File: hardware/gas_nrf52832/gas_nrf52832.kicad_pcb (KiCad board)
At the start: 2 copper layers, 64 x 35 mm, 73 parts, among them IC1 NPM1100-QDAA-R, IC2 TCK106AG,LF, J1 J-link, J2 USB4515-GF-A_REVA, J3 Batt_SW, J4 Conn_01x03, Q1 DMC2400UV, Q2 FDV303N, Q3 FDV303N, U3 LPV811DBV, U4 LPV812DGK, U5 BME680, X1 32.768kHz

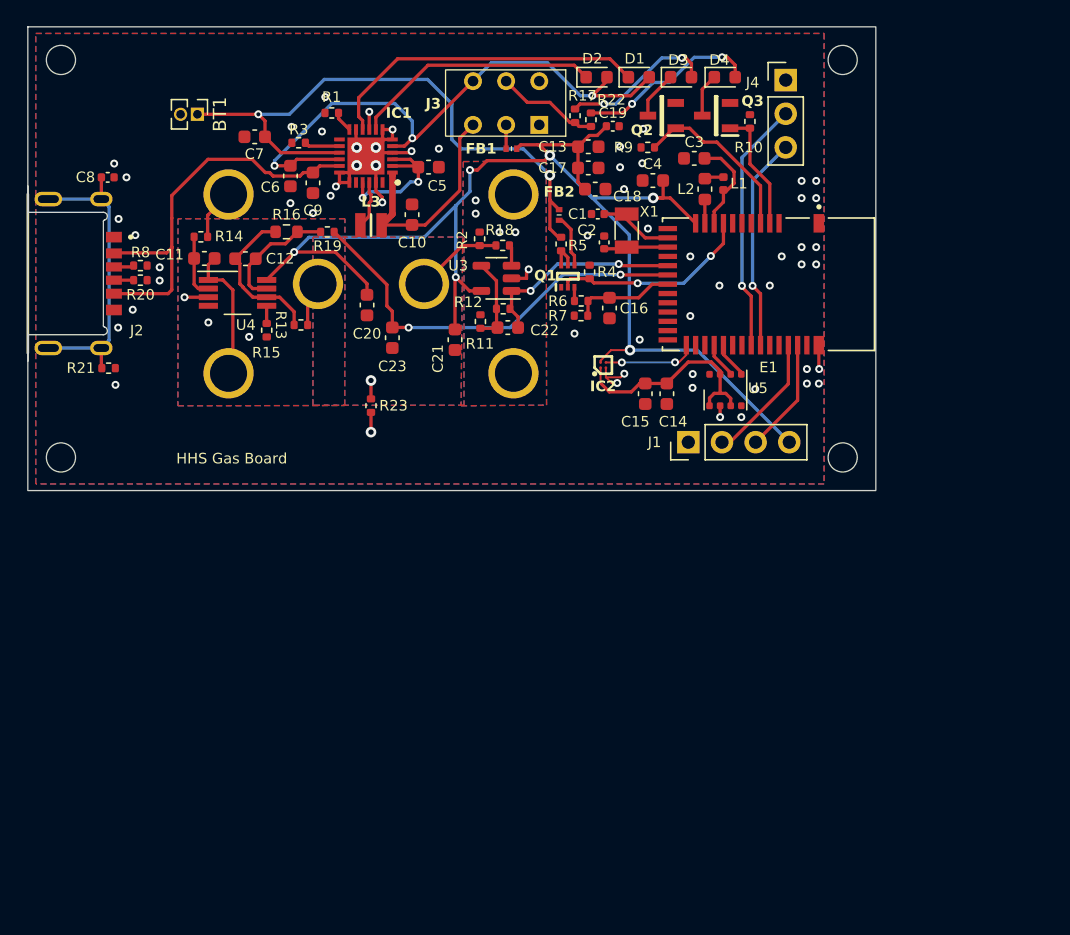
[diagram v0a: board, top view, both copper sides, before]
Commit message: hw: fix sensor circuit & fix ERC Error
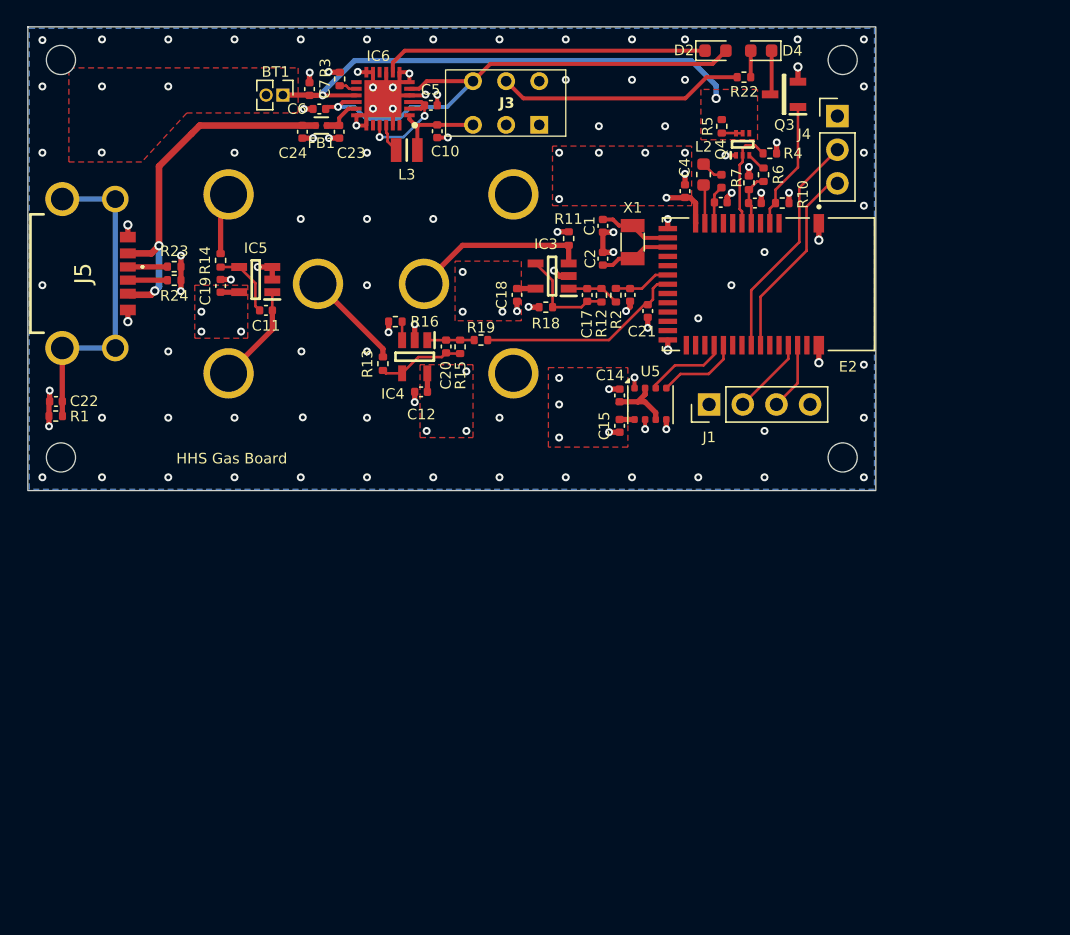
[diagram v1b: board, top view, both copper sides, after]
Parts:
- removed C8: 4.7nF, Capacitor_SMD:C_0402_1005Metric
- removed C9: 2.2uF, Capacitor_SMD:C_0603_1608Metric
- removed D1: L0603R, LED_SMD:LED_0603_1608Metric
- removed D3: L0603Y, LED_SMD:LED_0603_1608Metric
- removed E1: MDBT42Q-512KV2, MDBT42Q-512KV2:RAYTAC_MDBT42Q-512KV2
- removed FB2: BLM15PE121SH1D, BLM15PE121SH1D:NFZ15SG152SN10B
- removed IC1: NPM1100-QDAA-R, NPM1100-QDAA:QFN50P400X400X90-25N-D
- removed IC2: TCK106AG,LF, TCK106AG,LF:BGA4C40P2X2_79X79X59
- removed J2: USB4515-GF-A_REVA, USB4515-GF-A_REVA:GCT_USB4515-GF-A_REVA
- removed Q1: DMC2400UV, DMC2400UV:SOTFL50P162X60-6N
- removed Q2: FDV303N, FDV303N:SOT96P237X111-3N
- removed R17: 150, Resistor_SMD:R_0402_1005Metric
- removed R20, R8: 5.1k, Resistor_SMD:R_0402_1005Metric
- removed R21, R9: 1M, Resistor_SMD:R_0402_1005Metric
- removed U3: LPV811DBV, Package_TO_SOT_SMD:SOT-23-5
- removed U4: LPV812DGK, Package_SO:VSSOP-8_3.0x3.0mm_P0.65mm
- added C24: 100nF, Capacitor_SMD:C_0402_1005Metric, F.Cu at (110.1, 83.4)
- added E2: MDBT42Q-512KV2, MDBT42Q-512KV2:RAYTAC_MDBT42Q-512KV2, F.Cu at (145.3, 94.9)
- added IC3: LPV821DBVR, LPV821DBVR:SOT95P280X145-5N, F.Cu at (129.0, 94.3)
- added IC4: LPV821DBVR, LPV821DBVR:SOT95P280X145-5N, F.Cu at (118.6, 100.4)
- added IC5: LPV821DBVR, LPV821DBVR:SOT95P280X145-5N, F.Cu at (106.6, 94.6)
- added IC6: NPM1100-QDAA-R, NPM1100-QDAA-R:QFN50P400X400X90-25N-D, F.Cu at (116.2, 80.9)
- added J5: USB4515-GF-A, USB4515-GF-A_REVA:USB4515GFA, F.Cu at (93.0, 94.1)
- added Q4: DMC2400UV, DMC2400UV:SOTFL50P162X60-6N, F.Cu at (143.3, 84.4)
- added R24: 5.1k, Resistor_SMD:R_0402_1005Metric, F.Cu at (100.5, 94.6)
- C10, C11, C14, C15, C16, C18, C3, C4, C5, C6, C7: footprint Capacitor_SMD:C_0603_1608Metric -> Capacitor_SMD:C_0402_1005Metric
- C12: value 1.0uF -> 0.1uF; footprint Capacitor_SMD:C_0603_1608Metric -> Capacitor_SMD:C_0402_1005Metric
- C13: value 10uF -> 4.7uF; footprint Capacitor_SMD:C_0603_1608Metric -> Capacitor_SMD:C_0402_1005Metric
- C17: value 1.0uF -> 4.7uF; footprint Capacitor_SMD:C_0603_1608Metric -> Capacitor_SMD:C_0402_1005Metric
- C19: value 4.7nF -> 0.1uF
- C20: value 0.1uF -> 1.0uF; footprint Capacitor_SMD:C_0603_1608Metric -> Capacitor_SMD:C_0402_1005Metric
- C21: value 0.1uF -> 4.7uF; footprint Capacitor_SMD:C_0603_1608Metric -> Capacitor_SMD:C_0402_1005Metric
- C22: value 0.1uF -> 4.7nF; footprint Capacitor_SMD:C_0603_1608Metric -> Capacitor_SMD:C_0402_1005Metric
- C23: value 1.0uF -> 10nF; footprint Capacitor_SMD:C_0603_1608Metric -> Capacitor_SMD:C_0402_1005Metric
- FB1: value BLM15PE121SH1D -> 120R/0.9A; footprint BLM15PE121SH1D:NFZ15SG152SN10B -> MURATA_BLM15PE121SH1D:MURATA_BLM15PE121SH1D_0
- R1: value 0 -> 1M
- R11: value 10.7 -> 100
- R12: value 2k -> 2M
- R14: value 10 -> 10k
- R15: value 10 -> 150k
- R16: value 150k -> 10; footprint Resistor_SMD:R_0603_1608Metric -> Resistor_SMD:R_0402_1005Metric
- R18: value 10.7 -> 10k
- R19: value 49.9k -> 10k
- R2: value 100 -> 10k
- R23: value 0 -> 5.1k
- moved C22 34.6 mm to (91.5, 103.8)
- moved C19 32.0 mm to (104.0, 95.0), turned to -90 degrees
- moved R1 30.9 mm to (91.5, 104.9)
- moved R23 18.2 mm to (100.5, 93.6), turned to 0 degrees
- moved R6 16.7 mm to (144.9, 86.7), turned to 90 degrees
- moved C12 16.6 mm to (119.1, 103.0), turned to 0 degrees
- moved R4 16.3 mm to (145.4, 85.0), turned to 0 degrees
- moved R7 16.2 mm to (143.8, 87.3), turned to -90 degrees
- moved C23 16.1 mm to (112.9, 83.4)
- moved R5 15.0 mm to (141.8, 83.0)
- moved C21 14.7 mm to (136.2, 97.0)
- moved R15 14.6 mm to (122.0, 99.7), turned to -90 degrees
- moved FB1 14.5 mm to (111.5, 83.0)
- moved R19 14.2 mm to (123.6, 99.1)
- moved C16 13.5 mm to (144.3, 88.8), turned to 0 degrees
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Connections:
- C11 pad 1: Net-(U4A--) -> Net-(IC5-OUT)
- C11 pad 2: Net-(C11-Pad2) -> Net-(IC5--IN)
- C12 pad 1: Net-(C12-Pad1) -> GND
- C12 pad 2: Net-(U4B--) -> VDD_nRF
- C13 pad 1: VDD_nRF -> GND
- C13 pad 2: GND -> O2_MON
- C14 pad 2: VDD_BME -> VDD_nRF
- C15 pad 2: VDD_BME -> VDD_nRF
- C17 pad 1: VDD_nRF -> Net-(IC3-OUT)
- C17 pad 2: GND -> Net-(IC3--IN)
- C18 pad 1: VDD_nRF -> GND
- C18 pad 2: GND -> VDD_nRF
- C19 pad 1: VDD_nRF -> GND
- C19 pad 2: GND -> VDD_nRF
- C20 pad 1: GNDA -> Net-(IC4-OUT)
- C20 pad 2: VDD_nRF -> Net-(IC4--IN)
- C21 pad 1: GNDA -> GND
- C21 pad 2: VDD_nRF -> GAS_MON
- C22 pad 1: Net-(U3--) -> GND
- C22 pad 2: O2_MON -> Net-(C22-Pad2)
- C23 pad 1: GNDA -> GND
- C23 pad 2: GAS_MON -> VBUS
- FB1 pad 1: +3V0 -> Net-(J5-VBUS_1)
- FB1 pad 2: VDD_nRF -> VBUS
- J3 pad 2: +3V0 -> VDD_nRF
- R1 pad 1: Net-(IC1-ICHG) -> Net-(C22-Pad2)
- R11 pad 1: Net-(U3--) -> Net-(IC3-+IN)
- R11 pad 2: GNDA -> GND
- R12 pad 1: Net-(U3--) -> Net-(IC3-OUT)
- R12 pad 2: O2_MON -> Net-(IC3--IN)
- R13 pad 1: Net-(U4B--) -> Net-(IC4--IN)
- R14 pad 1: Net-(U4A--) -> Net-(IC5--IN)
- R15 pad 1: GNDA -> Net-(IC4-OUT)
- R15 pad 2: Net-(U4B-+) -> Net-(IC4--IN)
- R16 pad 1: Net-(C12-Pad1) -> Net-(IC4-+IN)
- R16 pad 2: Net-(U4B--) -> GND
- R18 pad 1: Net-(R18-Pad1) -> GND
- R18 pad 2: Net-(U3-+) -> Net-(IC3--IN)
- R19 pad 1: Net-(C12-Pad1) -> Net-(IC4-OUT)
- R2 pad 1: Net-(R18-Pad1) -> Net-(IC3-OUT)
- R2 pad 2: GNDA -> O2_MON
- R23 pad 1: GNDA -> Net-(J5-CC1)
- R6 pad 2: BAT_MON_TP -> Net-(Q4-D2)
- U1 pad +ve: Net-(R18-Pad1) -> Net-(IC3-+IN)
- U1 pad -ve: GNDA -> GND
- U2 pad C: Net-(C11-Pad2) -> Net-(IC5-OUT)
- U5 pad 2: VDD_BME -> VDD_nRF
- U5 pad 6: VDD_BME -> VDD_nRF
- U5 pad 8: VDD_BME -> VDD_nRF
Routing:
- net VDD_nRF: track 102.8 -> 14.3 mm, vias 6 -> 18
- net GND: track 31.1 -> 63.0 mm, vias 59 -> 112
- net VBUS: track 30.8 -> 3.11 mm
- net Net-(J5-VBUS_1): track 0.00 -> 27.7 mm, vias 0 -> 2
- net Net-(D1-K): track 24.7 -> 0.00 mm
- net Net-(C22-Pad2): track 0.00 -> 24.4 mm
- net Net-(C8-Pad2): track 22.9 -> 0.00 mm
- net VDD_BME: track 16.4 -> 0.00 mm
- net GAS_MON: track 31.5 -> 15.8 mm, vias 2 -> 0
- net Net-(IC3-+IN): track 0.00 -> 13.5 mm
- net LOW_BATT: track 13.2 -> 0.00 mm
- net Net-(U4B--): track 11.9 -> 0.00 mm
- net Net-(D4-A): track 13.8 -> 2.00 mm, vias 2 -> 0
- net Net-(D3-A): track 11.6 -> 0.00 mm, vias 2 -> 0
- net O2_MON: track 15.8 -> 4.51 mm, vias 2 -> 0
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- added copper zone on In1.Cu, net GND
- added copper zone on F.Cu, net VBAT
- added copper zone on F.Cu, net VDD_nRF
- added copper zone on In2.Cu, net VDD_nRF
- removed copper zone on F.Cu, net GND
- removed copper zone on B.Cu, net GNDA
- removed copper zone on F.Cu, net GNDA
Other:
- copper layers 2 -> 4

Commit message: feat: hw revision 1.0.2
Rev 1.0.2
- Oxygen Sensor
	- Voltage Amplification Ratio AdjustmentR18(10.7 -> 10k), R12(2.0k -> 2M)
	-> Reduce Current Consumption
	- Addition of lowpass filter for Noise Reduction
- Gas Sensor
	- Addition of lowpass filter for Noise Reduction
- 2 Layter -> 4 Layer
- hansam digitec requirement
	- If USB and RC are very close, errors may occur
	so increase the distance (R1, R23, R24, C22)
- BME680 Sensor Enable ctrl remove
- 32k Crystal Layout fix
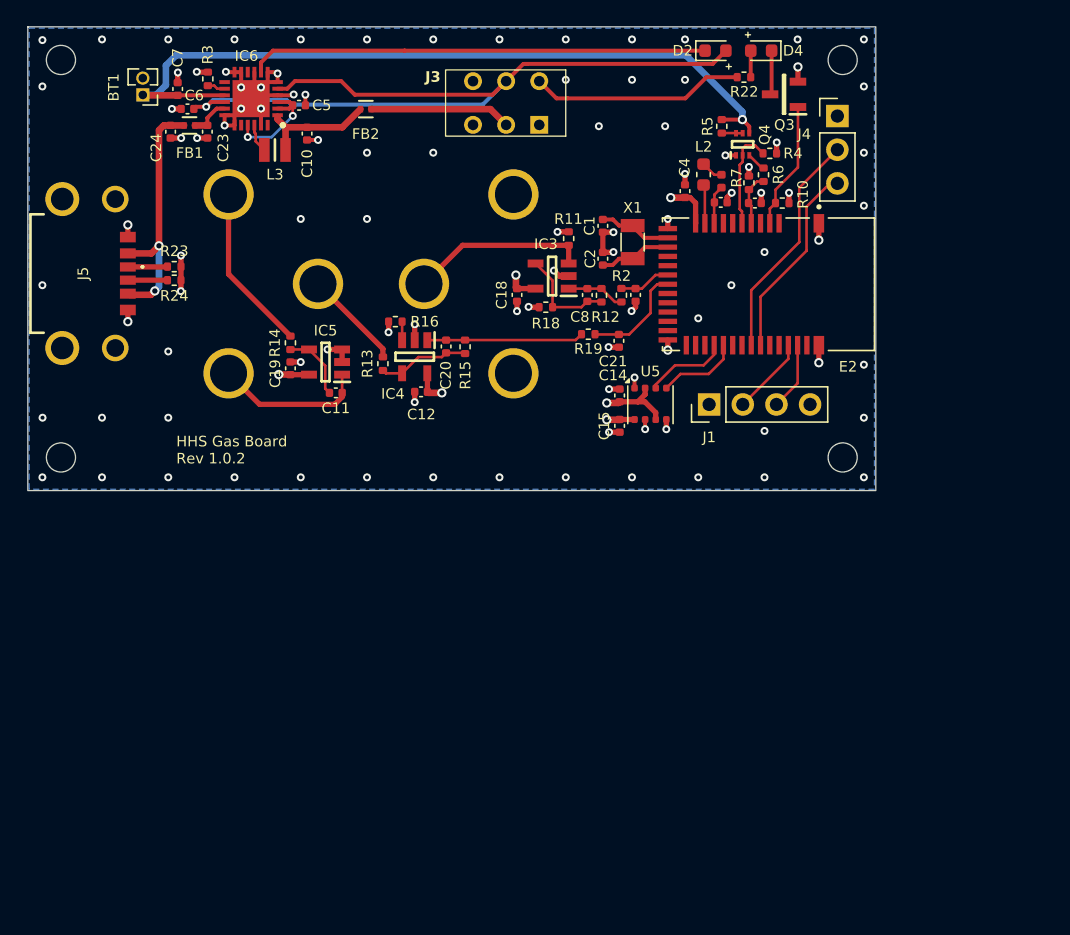
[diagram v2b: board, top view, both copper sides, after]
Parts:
- removed C17: 4.7uF, Capacitor_SMD:C_0402_1005Metric
- removed C22: 4.7nF, Capacitor_SMD:C_0402_1005Metric
- removed R1: 1M, Resistor_SMD:R_0402_1005Metric
- added C8: 1uF, Capacitor_SMD:C_0402_1005Metric, F.Cu at (131.6, 95.7)
- added FB2: 120R/0.9A, MURATA_BLM15PE121SH1D:MURATA_BLM15PE121SH1D_0, F.Cu at (114.9, 81.7)
- C11, C12, C14, C15, C16, C18, C19: value 0.1uF -> 100nF
- C13, C21: value 4.7uF -> 1uF
- C20, C3, C7: value 1.0uF -> 1uF
- D2: value L0603O -> L0603R
- Q4: value DMC2400UV -> DMC2400UV-7
- R14: value 10k -> 10
- R15: value 150k -> 100k
- R19, R2: value 10k -> 49.9k
- moved BT1 10.6 mm to (98.1, 80.6), turned to 180 degrees
- moved C23 9.95 mm to (103.0, 83.4)
- moved C24 9.95 mm to (100.2, 83.4)
- moved C6 9.95 mm to (101.5, 81.7)
- moved C7 9.95 mm to (100.7, 80.2)
- moved FB1 9.95 mm to (101.6, 82.9)
- moved IC6 9.95 mm to (106.2, 80.9)
- moved L3 9.95 mm to (108.0, 84.8)
- moved R3 9.95 mm to (103.0, 79.4)
- moved C5 9.95 mm to (109.9, 81.4)
- moved C10 9.83 mm to (110.5, 83.6)
- moved C19 8.16 mm to (109.2, 101.3)
- moved IC5 8.16 mm to (111.9, 100.8)
- moved C11 8.16 mm to (112.6, 103.1)
- moved R14 8.16 mm to (109.2, 99.3)
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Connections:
- E2 pad 25: SENSOR_EN -> unconnected-(E2-P0.11-Pad25)
- J3 pad 1: unconnected-(J3-Pin_1-Pad1) -> VDD_nRF
- J3 pad 2: VDD_nRF -> Net-(J3-Pin_2)
- J3 pad 3: Net-(IC6-VOUTB) -> unconnected-(J3-Pin_3-Pad3)
- J3 pad 4: unconnected-(J3-Pin_4-Pad4) -> VSYS
- J3 pad 5: VSYS -> VSYS_RAW
- J3 pad 6: VSYS_RAW -> unconnected-(J3-Pin_6-Pad6)
- J5 pad MH1: Net-(C22-Pad2) -> unconnected-(J5-PadMH1)
- J5 pad MH2: Net-(C22-Pad2) -> unconnected-(J5-PadMH2)
- J5 pad MH3: Net-(C22-Pad2) -> unconnected-(J5-PadMH3)
- J5 pad MH4: Net-(C22-Pad2) -> unconnected-(J5-PadMH4)
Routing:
- net Net-(C22-Pad2): track 24.4 -> 0.00 mm
- net VSYS_RAW: track 39.4 -> 62.1 mm
- net VBAT: track 38.3 -> 58.7 mm, vias 2 -> 1
- net Net-(J3-Pin_2): track 0.00 -> 10.7 mm
- net Net-(D2-K): track 24.7 -> 34.6 mm
- net Net-(J5-VBUS_1): track 27.7 -> 19.3 mm
- net Net-(IC4-OUT): track 3.54 -> 11.8 mm
- net Net-(R14-Pad2): track 4.71 -> 12.6 mm
- net GAS_MON: track 15.8 -> 8.05 mm
- net VDD_nRF: track 14.3 -> 19.0 mm, vias 18 -> 6
- net Net-(IC5-OUT): track 7.50 -> 11.6 mm
- net GND: track 63.0 -> 60.3 mm, vias 112 -> 99
- net VSYS: track 18.6 -> 16.1 mm
- net Net-(IC6-VOUTB): track 7.25 -> 9.01 mm
- removed copper zone on F.Cu, net VBAT
- removed copper zone on F.Cu, net VDD_nRF
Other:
- board text added: "HHS Gas Board Rev 1.0.2"
- board text removed: "HHS Gas Board"

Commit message: feat: hw revision 1.0.3
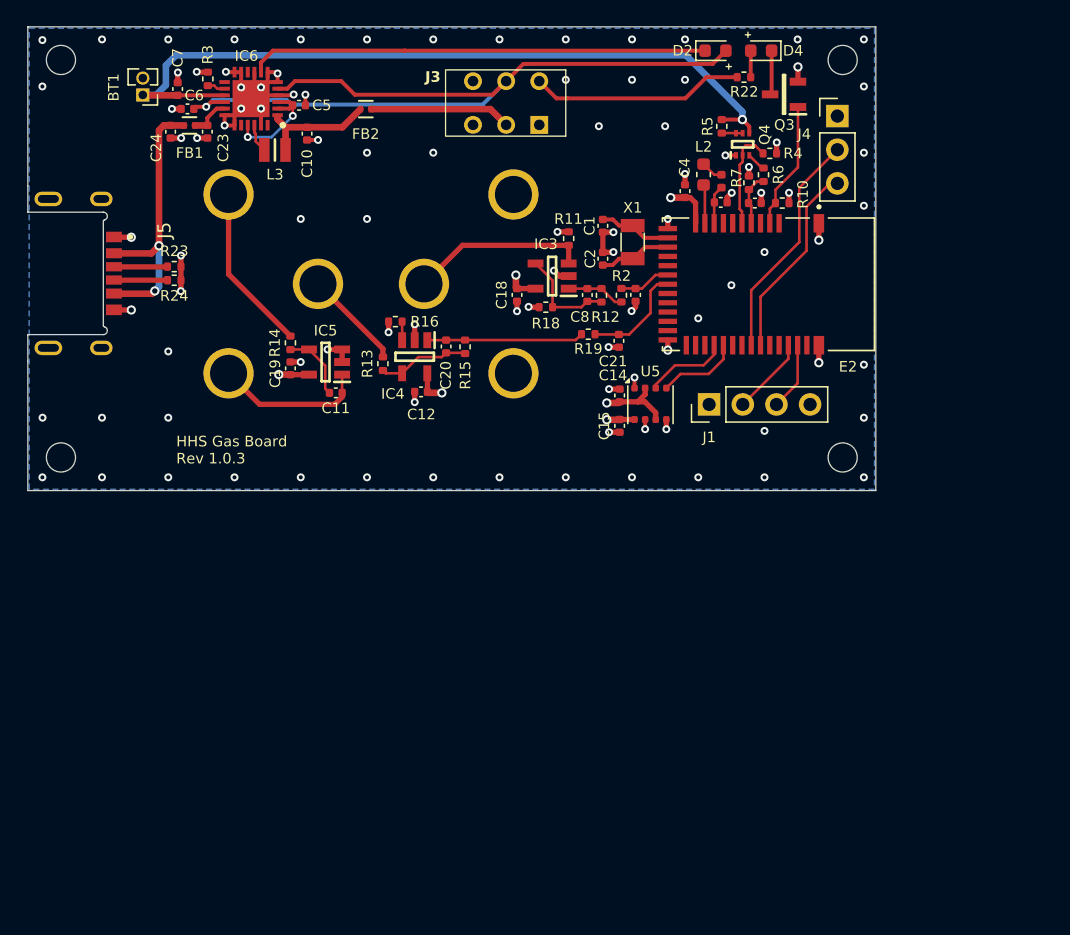
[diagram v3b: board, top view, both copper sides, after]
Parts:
- J5: footprint USB4515-GF-A_REVA:USB4515GFA -> USB4515-GF-A_REVA:GCT_USB4515-GF-A_REVA
- moved J5 2.05 mm to (91.0, 94.1)
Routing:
- net Net-(C24-Pad2): track 19.3 -> 21.1 mm
- net Net-(J5-CC2): track 2.99 -> 4.04 mm
- net Net-(J5-CC1): track 3.00 -> 4.05 mm
- net GND: track 60.3 -> 61.1 mm, vias 99 -> 98
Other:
- outline, holes or cut-outs redrawn
- board text added: "HHS Gas Board Rev 1.0.3"
- board text removed: "HHS Gas Board Rev 1.0.2"

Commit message: test: gas biasing circuit
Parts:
- added C17: 1uF, Capacitor_SMD:C_0402_1005Metric, F.Cu at (121.4, 84.6)
- added C22: 100nF, Capacitor_SMD:C_0402_1005Metric, F.Cu at (119.1, 86.3)
- added C25: 10uF, Capacitor_SMD:C_0402_1005Metric, F.Cu at (117.1, 97.7)
- added C26: 10uF, Capacitor_SMD:C_0402_1005Metric, F.Cu at (111.5, 98.2)
- added C27: 1uF, Capacitor_SMD:C_0402_1005Metric, F.Cu at (131.6, 84.1)
- added C28: 10uF, Capacitor_SMD:C_0402_1005Metric, F.Cu at (131.6, 82.9)
- added C9: 10uF, Capacitor_SMD:C_0402_1005Metric, F.Cu at (134.0, 101.3)
- added IC1: REF1112AIDBZR, REF1112AIDBZR:SOT95P237X112-3N, F.Cu at (116.2, 84.9)
- added R1: 49.9k, Resistor_SMD:R_0402_1005Metric, F.Cu at (114.7, 103.7)
- added R17: 9.1M, Resistor_SMD:R_0603_1608Metric, F.Cu at (121.7, 88.1)
- added R20: 0, Resistor_SMD:R_0402_1005Metric, F.Cu at (114.7, 91.1)
- added R21: 953k, Resistor_SMD:R_0603_1608Metric, F.Cu at (117.1, 89.3)
- added R25: 1M, Resistor_SMD:R_0402_1005Metric, F.Cu at (116.8, 87.5)
- added R26: 1M, Resistor_SMD:R_0402_1005Metric, F.Cu at (121.2, 85.8)
- added R27: NC, Resistor_SMD:R_0402_1005Metric, F.Cu at (119.3, 91.2)
- added R29: NC, Resistor_SMD:R_0402_1005Metric, F.Cu at (113.6, 98.2)
- added R31: 1M, Resistor_SMD:R_0402_1005Metric, F.Cu at (112.5, 87.9)
- added R8: 10k, Resistor_SMD:R_0402_1005Metric, F.Cu at (108.4, 104.0)
- added R9: 1M, Resistor_SMD:R_0402_1005Metric, F.Cu at (121.4, 89.7)
- added U3: MMBFJ177, MMBFJ177:SOT23, F.Cu at (109.4, 89.0)
- C13, C20, C21, C8: value 1uF -> 10uF
- C14, C15, Q4, R4, R5, R6, U5: moved to B.Cu
- J1: footprint Connector_PinHeader_2.54mm:PinHeader_1x04_P2.54mm_Vertical -> Connector_PinHeader_2.54mm:PinHeader_1x03_P2.54mm_Vertical
- R14: value 10 -> 10k
- R15: value 100k -> 300k
- R16: value 10 -> NC
- moved C14 8.83 mm to (142.2, 106.7)
- moved C15 8.83 mm to (142.2, 109.0)
- moved R4 8.73 mm to (136.7, 84.3), turned to -90 degrees
- moved Q4 7.63 mm to (136.0, 82.3), turned to 180 degrees
- moved R5 7.49 mm to (134.7, 80.7), turned to 0 degrees
- moved J1 6.92 mm to (146.3, 108.2), turned to 180 degrees
- moved R6 6.91 mm to (139.2, 82.8), turned to 180 degrees
- moved R16 5.95 mm to (117.0, 91.8)
- moved U5 4.87 mm to (139.9, 107.3), turned to 180 degrees
- moved R22 2.98 mm to (140.5, 79.6)
- moved D2 2.30 mm to (139.0, 77.0)
- moved D4 2.30 mm to (142.5, 77.0)
- moved Q3 2.16 mm to (144.3, 80.2)
- moved J4 2.01 mm to (148.5, 82.0)
- moved R10 0.88 mm to (145.8, 88.1), turned to -90 degrees
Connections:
- E2 pad 7: unconnected-(E2-P0.30/AIN6-Pad7) -> POTENTIOSTAT_OUT
- IC4 pad 3: Net-(IC4-+IN) -> Vref
- IC5 pad 3: GND -> Vref
- R16 pad 1: Net-(IC4-+IN) -> Vref
- U2 pad C: Net-(IC5-OUT) -> Net-(R8-Pad2)
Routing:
- net POTENTIOSTAT_OUT: track 0.00 -> 35.3 mm, vias 0 -> 2
- net Vref: track 0.00 -> 21.9 mm, vias 0 -> 2
- net VDD_nRF: track 19.0 -> 29.5 mm, vias 6 -> 8
- net VBAT: track 58.7 -> 48.9 mm, vias 1 -> 0
- net GND: track 61.1 -> 68.5 mm, vias 98 -> 87
- net BAT_MON: track 3.99 -> 11.1 mm, vias 0 -> 1
- net Net-(R13-Pad2): track 7.54 -> 14.6 mm
- net BAT_MON_EN: track 7.70 -> 13.9 mm, vias 0 -> 1
- net Net-(IC1-VO): track 0.00 -> 5.06 mm
- net Net-(R8-Pad2): track 0.00 -> 4.31 mm
- net VSYS: track 16.1 -> 12.0 mm
- net Vref_REF: track 0.00 -> 3.94 mm
- net Net-(IC5-OUT): track 11.6 -> 7.73 mm
- net Vref_Devider: track 0.00 -> 3.59 mm
- net SCL: track 6.27 -> 8.91 mm, vias 0 -> 1
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- added copper zone on F.Cu, net GND

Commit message: feat: hw revision 1.0.4
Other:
- board text added: "HHS Gas Board Rev 1.0.4"
- board text removed: "HHS Gas Board Rev 1.0.3"
